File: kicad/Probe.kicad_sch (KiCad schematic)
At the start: 0 parts

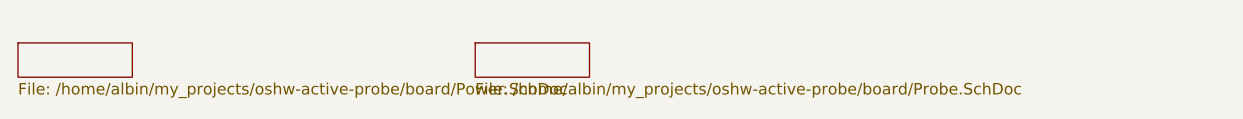
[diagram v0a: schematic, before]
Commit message: Add missing sheets
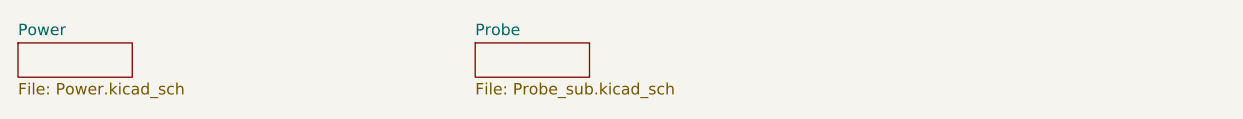
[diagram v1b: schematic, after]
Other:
- sheet  renamed Probe
- added sheet Power (Power.kicad_sch)
- sheet Probe: file /home/albin/my_projects/oshw-active-probe/board/Probe.SchDoc -> Probe_sub.kicad_sch
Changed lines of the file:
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@@
 			(color 0 0 0 0.0000)
 		)
-		(property "Sheetname" ""
+		(property "Sheetname" "Power"
 			(at 25.4 24.6884 0)
 			(effects
@@
 			)
 		)
-		(property "Sheetfile" "/home/albin/my_projects/oshw-active-probe/board/Power.SchDoc"
+		(property "Sheetfile" "Power.kicad_sch"
 			(at 25.4 29.7946 0)
 			(effects
@@
 			(color 0 0 0 0.0000)
 		)
-		(property "Sheetname" ""
+		(property "Sheetname" "Probe"
 			(at 76.2 24.6884 0)
 			(effects
@@
 			)
 		)
-		(property "Sheetfile" "/home/albin/my_projects/oshw-active-probe/board/Probe.SchDoc"
+		(property "Sheetfile" "Probe_sub.kicad_sch"
 			(at 76.2 29.7946 0)
 			(effects
